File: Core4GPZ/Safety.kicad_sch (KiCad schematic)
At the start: 6 parts

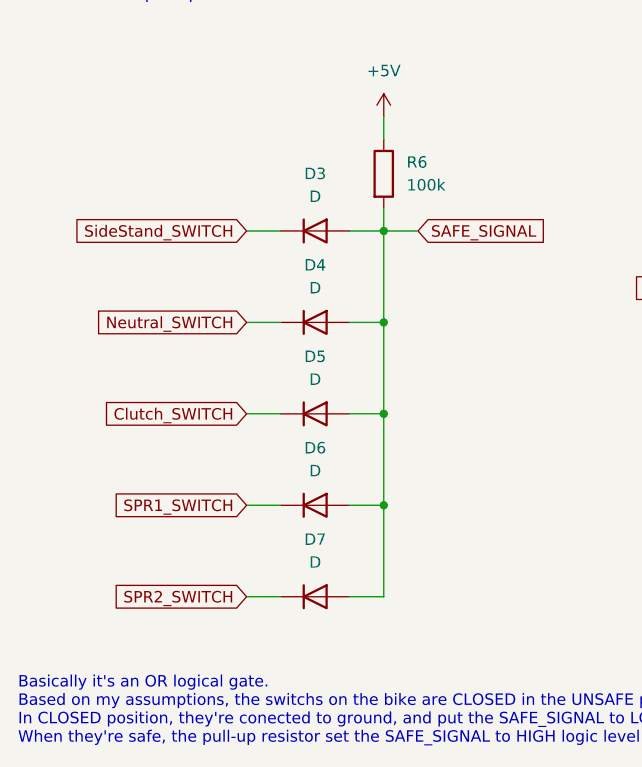
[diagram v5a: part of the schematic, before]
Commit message: Started Implementation of VR Conditionner
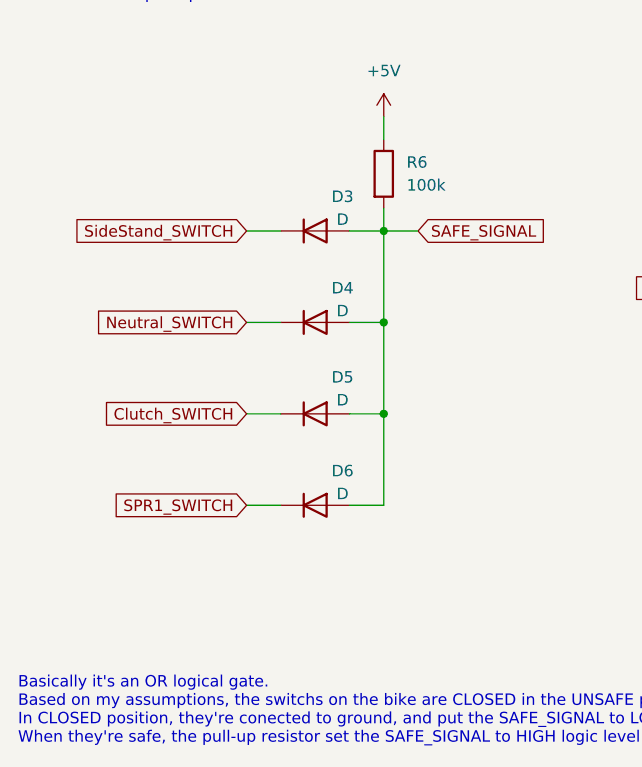
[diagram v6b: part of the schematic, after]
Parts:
- removed D7: D, Diode_THT:D_DO-35_SOD27_P2.54mm_Vertical_KathodeUp, symbol Device:D
- D3, D4, D5, D6: footprint Diode_THT:D_DO-35_SOD27_P2.54mm_Vertical_KathodeUp -> Diode_SMD:D_0603_1608Metric
- R6: footprint Resistor_THT:R_Axial_DIN0204_L3.6mm_D1.6mm_P5.08mm_Horizontal -> Resistor_SMD:R_0603_1608Metric
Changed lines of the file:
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@@
 	(paper "A4")
 	(junction
-		(at 55.88 74.93)
-		(diameter 0)
-		(color 0 0 0 0)
-	)
-	(junction
 		(at 55.88 64.77)
 		(diameter 0)
@@
 	(wire
 		(pts
-			(xy 40.64 85.09) (xy 44.45 85.09)
-		)
-		(stroke
-			(width 0)
-			(type default)
-		)
-	)
-	(wire
-		(pts
 			(xy 52.07 54.61) (xy 55.88 54.61)
 		)
@@
 	(wire
 		(pts
-			(xy 52.07 85.09) (xy 55.88 85.09)
-		)
-		(stroke
-			(width 0)
-			(type default)
-		)
-	)
-	(wire
-		(pts
 			(xy 55.88 44.45) (xy 55.88 54.61)
 		)
@@
 		)
 	)
-	(wire
-		(pts
-			(xy 55.88 85.09) (xy 55.88 74.93)
-		)
-		(stroke
-			(width 0)
-			(type default)
-		)
-	)
 	(image
 		(at 213.36 88.9)
@@
 		)
 	)
-	(global_label "SPR2_SWITCH"
-		(shape input)
-		(at 40.64 85.09 180)
-		(fields_autoplaced yes)
-		(effects
-			(font
-				(size 1.27 1.27)
-			)
-			(justify right)
-		)
-		(property "Intersheetrefs" "${INTERSHEET_REFS}"
-			(at 24.8944 85.09 0)
-			(effects
-				(font
-					(size 1.27 1.27)
-				)
-				(justify right)
-				(hide yes)
-			)
-		)
-	)
 	(global_label "SPR1_SWITCH"
 		(shape input)
@@
 			)
 		)
-		(property "Footprint" "Resistor_THT:R_Axial_DIN0204_L3.6mm_D1.6mm_P5.08mm_Horizontal"
+		(property "Footprint" "Resistor_SMD:R_0603_1608Metric"
 			(at 54.102 38.1 90)
 			(effects
@@
 	(symbol
 		(lib_id "Device:D")
-		(at 48.26 64.77 0)
+		(at 48.26 44.45 0)
 		(unit 1)
 		(exclude_from_sim no)
@@
 		(on_board yes)
 		(dnp no)
-		(fields_autoplaced yes)
-		(property "Reference" "D5"
-			(at 48.26 58.42 0)
+		(property "Reference" "D3"
+			(at 51.308 40.64 0)
 			(effects
 				(font
@@
 		)
 		(property "Value" "D"
-			(at 48.26 60.96 0)
+			(at 51.308 43.18 0)
 			(effects
 				(font
@@
 			)
 		)
-		(property "Footprint" "Diode_THT:D_DO-35_SOD27_P2.54mm_Vertical_KathodeUp"
-			(at 48.26 64.77 0)
+		(property "Footprint" "Diode_SMD:D_0603_1608Metric"
+			(at 48.26 44.45 0)
 			(effects
 				(font
@@
 		)
 		(property "Datasheet" "~"
-			(at 48.26 64.77 0)
+			(at 48.26 44.45 0)
 			(effects
 				(font
@@
 		)
 		(property "Description" ""
-			(at 48.26 64.77 0)
+			(at 48.26 44.45 0)
 			(effects
 				(font
@@
 		)
 		(property "Sim.Device" "D"
-			(at 48.26 64.77 0)
+			(at 48.26 44.45 0)
 			(effects
 				(font
@@
 		)
 		(property "Sim.Pins" "1=K 2=A"
-			(at 48.26 64.77 0)
+			(at 48.26 44.45 0)
 			(effects
 				(font
@@
 			(project "Core4GPZ"
 				(path "/ac28f42d-34b3-4fcc-84dd-ab6106f99610/47dee9fe-f537-47a7-b917-fe922e75e357"
-					(reference "D5")
+					(reference "D3")
 					(unit 1)
 				)
@@
 		(on_board yes)
 		(dnp no)
-		(fields_autoplaced yes)
 		(property "Reference" "D4"
-			(at 48.26 48.26 0)
+			(at 51.308 50.8 0)
 			(effects
 				(font
@@
 		)
 		(property "Value" "D"
-			(at 48.26 50.8 0)
+			(at 51.308 53.34 0)
 			(effects
 				(font
@@
 			)
 		)
-		(property "Footprint" "Diode_THT:D_DO-35_SOD27_P2.54mm_Vertical_KathodeUp"
+		(property "Footprint" "Diode_SMD:D_0603_1608Metric"
 			(at 48.26 54.61 0)
 			(effects
@@
 	(symbol
 		(lib_id "Device:D")
-		(at 48.26 44.45 0)
+		(at 48.26 74.93 0)
 		(unit 1)
 		(exclude_from_sim no)
@@
 		(on_board yes)
 		(dnp no)
-		(fields_autoplaced yes)
-		(property "Reference" "D3"
-			(at 48.26 38.1 0)
+		(property "Reference" "D6"
+			(at 51.308 71.12 0)
 			(effects
 				(font
@@
 		)
 		(property "Value" "D"
-			(at 48.26 40.64 0)
+			(at 51.308 73.66 0)
 			(effects
 				(font
@@
 			)
 		)
-		(property "Footprint" "Diode_THT:D_DO-35_SOD27_P2.54mm_Vertical_KathodeUp"
-			(at 48.26 44.45 0)
+		(property "Footprint" "Diode_SMD:D_0603_1608Metric"
+			(at 48.26 74.93 0)
 			(effects
 				(font
@@
 		)
 		(property "Datasheet" "~"
-			(at 48.26 44.45 0)
+			(at 48.26 74.93 0)
 			(effects
 				(font
@@
 		)
 		(property "Description" ""
-			(at 48.26 44.45 0)
+			(at 48.26 74.93 0)
 			(effects
 				(font
@@
 		)
 		(property "Sim.Device" "D"
-			(at 48.26 44.45 0)
+			(at 48.26 74.93 0)
 			(effects
 				(font
@@
 		)
 		(property "Sim.Pins" "1=K 2=A"
-			(at 48.26 44.45 0)
+			(at 48.26 74.93 0)
 			(effects
 				(font
@@
 			(project "Core4GPZ"
 				(path "/ac28f42d-34b3-4fcc-84dd-ab6106f99610/47dee9fe-f537-47a7-b917-fe922e75e357"
-					(reference "D3")
+					(reference "D6")
 					(unit 1)
 				)
@@
 	)
 	(symbol
-		(lib_id "Device:D")
-		(at 48.26 74.93 0)
+		(lib_id "power:+5V")
+		(at 55.88 31.75 0)
 		(unit 1)
 		(exclude_from_sim no)
@@
 		(dnp no)
 		(fields_autoplaced yes)
-		(property "Reference" "D6"
-			(at 48.26 68.58 0)
-			(effects
-				(font
-					(size 1.27 1.27)
-				)
-			)
-		)
-		(property "Value" "D"
-			(at 48.26 71.12 0)
-			(effects
-				(font
-					(size 1.27 1.27)
-				)
-			)
-		)
-		(property "Footprint" "Diode_THT:D_DO-35_SOD27_P2.54mm_Vertical_KathodeUp"
-			(at 48.26 74.93 0)
+		(property "Reference" "#PWR013"
+			(at 55.88 35.56 0)
 			(effects
 				(font
@@
 			)
 		)
-		(property "Datasheet" "~"
-			(at 48.26 74.93 0)
+		(property "Value" "+5V"
+			(at 55.88 26.67 0)
 			(effects
 				(font
 					(size 1.27 1.27)
 				)
-				(hide yes)
 			)
 		)
-		(property "Description" ""
-			(at 48.26 74.93 0)
+		(property "Footprint" ""
+			(at 55.88 31.75 0)
 			(effects
 				(font
@@
 			)
 		)
-		(property "Sim.Device" "D"
-			(at 48.26 74.93 0)
+		(property "Datasheet" ""
+			(at 55.88 31.75 0)
 			(effects
 				(font
@@
 			)
 		)
-		(property "Sim.Pins" "1=K 2=A"
-			(at 48.26 74.93 0)
+		(property "Description" ""
+			(at 55.88 31.75 0)
 			(effects
 				(font
@@
 			)
 		)
-		(pin "2"
-		)
 		(pin "1"
 		)
@@
 			(project "Core4GPZ"
 				(path "/ac28f42d-34b3-4fcc-84dd-ab6106f99610/47dee9fe-f537-47a7-b917-fe922e75e357"
-					(reference "D6")
+					(reference "#PWR013")
 					(unit 1)
 				)
@@
 	(symbol
 		(lib_id "Device:D")
-		(at 48.26 85.09 0)
+		(at 48.26 64.77 0)
 		(unit 1)
 		(exclude_from_sim no)
@@
 		(on_board yes)
 		(dnp no)
-		(fields_autoplaced yes)
-		(property "Reference" "D7"
-			(at 48.26 78.74 0)
+		(property "Reference" "D5"
+			(at 51.308 60.706 0)
 			(effects
 				(font
@@
 		)
 		(property "Value" "D"
-			(at 48.26 81.28 0)
+			(at 51.308 63.246 0)
 			(effects
 				(font
@@
 			)
 		)
-		(property "Footprint" "Diode_THT:D_DO-35_SOD27_P2.54mm_Vertical_KathodeUp"
-			(at 48.26 85.09 0)
+		(property "Footprint" "Diode_SMD:D_0603_1608Metric"
+			(at 48.26 64.77 0)
 			(effects
 				(font
@@
 		)
 		(property "Datasheet" "~"
-			(at 48.26 85.09 0)
+			(at 48.26 64.77 0)
 			(effects
 				(font
@@
 		)
 		(property "Description" ""
-			(at 48.26 85.09 0)
+			(at 48.26 64.77 0)
 			(effects
 				(font
@@
 		)
 		(property "Sim.Device" "D"
-			(at 48.26 85.09 0)
+			(at 48.26 64.77 0)
 			(effects
 				(font
@@
 		)
 		(property "Sim.Pins" "1=K 2=A"
-			(at 48.26 85.09 0)
+			(at 48.26 64.77 0)
 			(effects
 				(font
@@
 			(project "Core4GPZ"
 				(path "/ac28f42d-34b3-4fcc-84dd-ab6106f99610/47dee9fe-f537-47a7-b917-fe922e75e357"
-					(reference "D7")
-					(unit 1)
-				)
-			)
-		)
-	)
-	(symbol
-		(lib_id "power:+5V")
-		(at 55.88 31.75 0)
-		(unit 1)
-		(exclude_from_sim no)
-		(in_bom yes)
-		(on_board yes)
-		(dnp no)
-		(fields_autoplaced yes)
-		(property "Reference" "#PWR013"
-			(at 55.88 35.56 0)
-			(effects
-				(font
-					(size 1.27 1.27)
-				)
-				(hide yes)
-			)
-		)
-		(property "Value" "+5V"
-			(at 55.88 26.67 0)
-			(effects
-				(font
-					(size 1.27 1.27)
-				)
-			)
-		)
-		(property "Footprint" ""
-			(at 55.88 31.75 0)
-			(effects
-				(font
-					(size 1.27 1.27)
-				)
-				(hide yes)
-			)
-		)
-		(property "Datasheet" ""
-			(at 55.88 31.75 0)
-			(effects
-				(font
-					(size 1.27 1.27)
-				)
-				(hide yes)
-			)
-		)
-		(property "Description" ""
-			(at 55.88 31.75 0)
-			(effects
-				(font
-					(size 1.27 1.27)
-				)
-				(hide yes)
-			)
-		)
-		(pin "1"
-		)
-		(instances
-			(project "Core4GPZ"
-				(path "/ac28f42d-34b3-4fcc-84dd-ab6106f99610/47dee9fe-f537-47a7-b917-fe922e75e357"
-					(reference "#PWR013")
+					(reference "D5")
 					(unit 1)
 				)
